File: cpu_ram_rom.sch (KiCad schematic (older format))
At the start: 10 parts, among them SW2 Reset, U6 SRAM - IS62C5128BL-45TLI, U7 SST39SF040, U8 CPU -Z84C0020AEG, U9 DS1813R-5+T&R

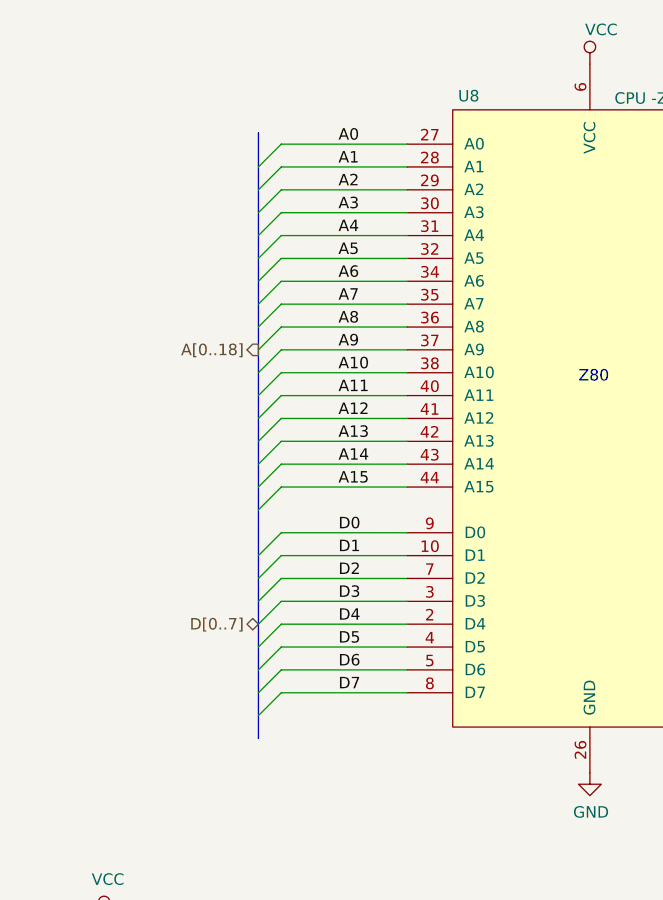
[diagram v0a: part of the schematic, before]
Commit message: fixed bus connections
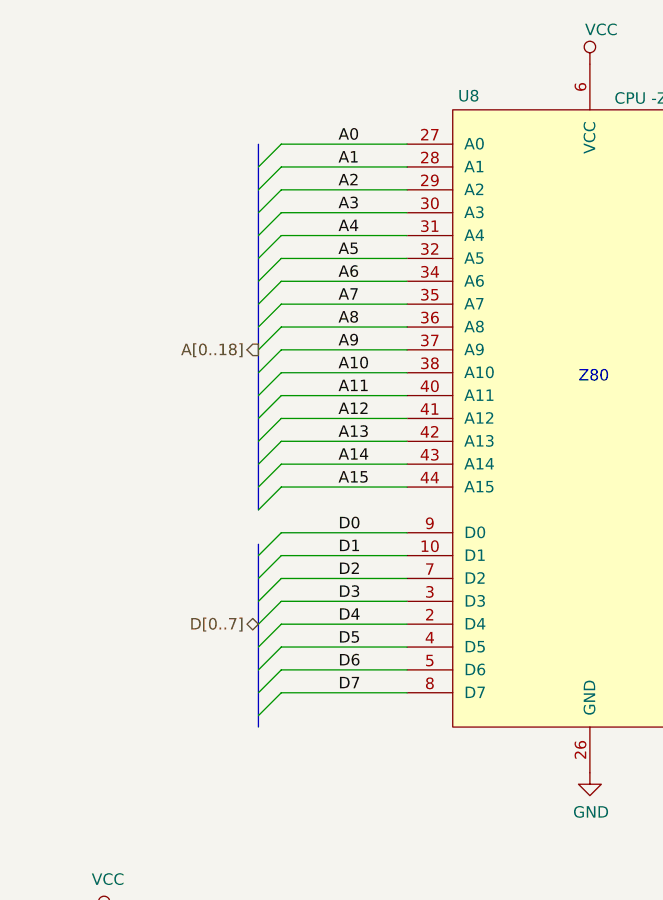
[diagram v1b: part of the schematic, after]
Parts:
- SW2: footprint Button_Switch_SMD:SW_Push_SPST_NO_Alps_SKRK -> Button_Switch_SMD:SW_SPST_FSMSM
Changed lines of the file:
@@
 F 0 "SW2" V 4004 5913 50  0000 L CNN
 F 1 "Reset" V 4095 5913 50  0000 L CNN
-F 2 "Button_Switch_SMD:SW_Push_SPST_NO_Alps_SKRK" H 4050 5965 50  0001 C CNN
+F 2 "Button_Switch_SMD:SW_SPST_FSMSM" H 4050 5965 50  0001 C CNN
 F 3 "~" H 4050 5965 50  0001 C CNN
 	1    4050 5765
@@
 ROM_~CE~
 Wire Bus Line
-	2000 1500 2000 4150
+	2000 3300 2000 4100
+Wire Bus Line
+	2000 1550 2000 3150
 $EndSCHEMATC

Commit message: passed DRC
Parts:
- removed R54, R55, R56, R57: 10K, Resistor_SMD:R_0603_1608Metric_Pad1.05x0.95mm_HandSolder, symbol Device:R_Small
- removed SW2: Reset, Button_Switch_SMD:SW_SPST_FSMSM, symbol Switch:SW_Push
- removed U6: SRAM - IS62C5128BL-45TLI, Package_SO:TSOP-II-32_21.0x10.2mm_P1.27mm, symbol THS-80:IS62C5128BL-45TLI
- removed U8: CPU -Z84C0020AEG, Package_QFP:LQFP-44_10x10mm_P0.8mm, symbol THS-80:Z84C0010AEG
- removed U9: DS1813R-5+T&R, Package_TO_SOT_SMD:SOT-23, symbol THS-80:DS1813R-5+T&R
- added C16, C17, C18: 100nF, Capacitor_SMD:C_0603_1608Metric_Pad1.05x0.95mm_HandSolder, symbol Device:C_Small
- added U4: Z84C0010AEG, Package_QFP:LQFP-44_10x10mm_P0.8mm, symbol THS-80:Z84C0010AEG
- added U5: IS62C5128BL-45TLI, Package_SO:TSOP-II-32_21.0x10.2mm_P1.27mm, symbol THS-80:IS62C5128BL-45TLI
- renumbered R53 to R21, U7 to U6
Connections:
- net labels removed: RAM_~CE, ~BUSREQ
- wire segments 116 -> 104
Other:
- note removed: "SRAM 512Kx8"
- note removed: "Z80"
- moved on the sheet: R21, U6

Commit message: finished routing, drc passed
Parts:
- added D13, D14: GRN, LED_SMD:LED_0603_1608Metric_Pad1.05x0.95mm_HandSolder, symbol Device:LED
- added R19, R20: 10K, Resistor_SMD:R_0603_1608Metric_Pad1.05x0.95mm_HandSolder, symbol Device:R_Small
- added R40, R41: 360R, Resistor_SMD:R_0603_1608Metric_Pad1.05x0.95mm_HandSolder, symbol Device:R_Small
- added U12: 74HCT3G04, Package_SO:TSSOP-8_3x3mm_P0.65mm, symbol 74xGxx:74HCT3G04
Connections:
- net labels added: RAM_~CE, ROM_~CE
- wire segments 104 -> 107
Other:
- moved on the sheet: C16, C17, C18, R21, U4, U5, U6

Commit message: track cleanup, fixed slots in ground plane
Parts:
- U12: symbol 74xGxx:74HCT3G04 -> THS-80-rescue:74HCT3G04-74xGxx
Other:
- moved on the sheet: D13, D14, R19, R20, R40, R41
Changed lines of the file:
@@
 L power:GND #PWR?
 U 1 1 5D949AED
-P 9100 5150
+P 9800 5150
 AR Path="/5D84B1E0/5D949AED" Ref="#PWR?"  Part="1"
 AR Path="/5D6224DC/5D949AED" Ref="#PWR081"  Part="1"
-F 0 "#PWR081" H 9100 4900 50  0001 C CNN
-F 1 "GND" H 9105 4977 50  0000 C CNN
-F 2 "" H 9100 5150 50  0001 C CNN
-F 3 "" H 9100 5150 50  0001 C CNN
-	1    9100 5150
+F 0 "#PWR081" H 9800 4900 50  0001 C CNN
+F 1 "GND" H 9805 4977 50  0000 C CNN
+F 2 "" H 9800 5150 50  0001 C CNN
+F 3 "" H 9800 5150 50  0001 C CNN
+	1    9800 5150
 	1    0    0    -1
 $EndComp
 Wire Wire Line
-	8550 4650 7950 4650
-Text Label 8200 4650 0    50   ~ 0
+	9250 4650 8650 4650
+Text Label 8900 4650 0    50   ~ 0
 ROM_~CE
 $Comp
 L power:GND #PWR?
 U 1 1 5D949B01
-P 6550 5100
+P 6550 5150
 AR Path="/5D84B1E0/5D949B01" Ref="#PWR?"  Part="1"
 AR Path="/5D6224DC/5D949B01" Ref="#PWR078"  Part="1"
-F 0 "#PWR078" H 6550 4850 50  0001 C CNN
-F 1 "GND" H 6555 4927 50  0000 C CNN
-F 2 "" H 6550 5100 50  0001 C CNN
-F 3 "" H 6550 5100 50  0001 C CNN
-	1    6550 5100
+F 0 "#PWR078" H 6550 4900 50  0001 C CNN
+F 1 "GND" H 6555 4977 50  0000 C CNN
+F 2 "" H 6550 5150 50  0001 C CNN
+F 3 "" H 6550 5150 50  0001 C CNN
+	1    6550 5150
 	1    0    0    -1
 $EndComp
 Wire Wire Line
-	6000 4600 5400 4600
-Text Label 5650 4600 0    50   ~ 0
+	6000 4650 5400 4650
+Text Label 5650 4650 0    50   ~ 0
 RAM_~CE
 $Comp
 L Device:R_Small R?
 U 1 1 5D949B09
-P 6550 5000
+P 6550 5050
 AR Path="/5D84B1E0/5D949B09" Ref="R?"  Part="1"
 AR Path="/5D6224DC/5D949B09" Ref="R40"  Part="1"
-F 0 "R40" H 6609 5046 50  0000 L CNN
-F 1 "360R" H 6609 4955 50  0000 L CNN
-F 2 "Resistor_SMD:R_0603_1608Metric_Pad1.05x0.95mm_HandSolder" H 6550 5000 50  0001 C CNN
-F 3 "~" H 6550 5000 50  0001 C CNN
-	1    6550 5000
+F 0 "R40" H 6609 5096 50  0000 L CNN
+F 1 "360R" H 6609 5005 50  0000 L CNN
+F 2 "Resistor_SMD:R_0603_1608Metric_Pad1.05x0.95mm_HandSolder" H 6550 5050 50  0001 C CNN
+F 3 "~" H 6550 5050 50  0001 C CNN
+	1    6550 5050
 	-1   0    0    1
 $EndComp
@@
 L Device:LED D?
 U 1 1 5D949B0F
-P 6550 4750
+P 6550 4800
 AR Path="/5D84B1E0/5D949B0F" Ref="D?"  Part="1"
 AR Path="/5D6224DC/5D949B0F" Ref="D13"  Part="1"
-F 0 "D13" V 6589 4633 50  0000 R CNN
-F 1 "GRN" V 6498 4633 50  0000 R CNN
-F 2 "LED_SMD:LED_0603_1608Metric_Pad1.05x0.95mm_HandSolder" H 6550 4750 50  0001 C CNN
-F 3 "~" H 6550 4750 50  0001 C CNN
-	1    6550 4750
+F 0 "D13" V 6589 4683 50  0000 R CNN
+F 1 "GRN" V 6498 4683 50  0000 R CNN
+F 2 "LED_SMD:LED_0603_1608Metric_Pad1.05x0.95mm_HandSolder" H 6550 4800 50  0001 C CNN
+F 3 "~" H 6550 4800 50  0001 C CNN
+	1    6550 4800
 	0    -1   -1   0
 $EndComp
@@
 L Device:LED D?
 U 1 1 5D949B15
-P 9100 4800
+P 9800 4800
 AR Path="/5D84B1E0/5D949B15" Ref="D?"  Part="1"
 AR Path="/5D6224DC/5D949B15" Ref="D14"  Part="1"
-F 0 "D14" V 9139 4683 50  0000 R CNN
-F 1 "GRN" V 9048 4683 50  0000 R CNN
-F 2 "LED_SMD:LED_0603_1608Metric_Pad1.05x0.95mm_HandSolder" H 9100 4800 50  0001 C CNN
-F 3 "~" H 9100 4800 50  0001 C CNN
-	1    9100 4800
+F 0 "D14" V 9839 4683 50  0000 R CNN
+F 1 "GRN" V 9748 4683 50  0000 R CNN
+F 2 "LED_SMD:LED_0603_1608Metric_Pad1.05x0.95mm_HandSolder" H 9800 4800 50  0001 C CNN
+F 3 "~" H 9800 4800 50  0001 C CNN
+	1    9800 4800
 	0    -1   -1   0
 $EndComp
@@
 L Device:R_Small R?
 U 1 1 5D949B1B
-P 9100 5050
+P 9800 5050
 AR Path="/5D84B1E0/5D949B1B" Ref="R?"  Part="1"
 AR Path="/5D6224DC/5D949B1B" Ref="R41"  Part="1"
-F 0 "R41" H 9159 5096 50  0000 L CNN
-F 1 "360R" H 9159 5005 50  0000 L CNN
-F 2 "Resistor_SMD:R_0603_1608Metric_Pad1.05x0.95mm_HandSolder" H 9100 5050 50  0001 C CNN
-F 3 "~" H 9100 5050 50  0001 C CNN
-	1    9100 5050
+F 0 "R41" H 9859 5096 50  0000 L CNN
+F 1 "360R" H 9859 5005 50  0000 L CNN
+F 2 "Resistor_SMD:R_0603_1608Metric_Pad1.05x0.95mm_HandSolder" H 9800 5050 50  0001 C CNN
+F 3 "~" H 9800 5050 50  0001 C CNN
+	1    9800 5050
 	-1   0    0    1
 $EndComp
@@
 L Device:R_Small R20
 U 1 1 5D959555
-P 7950 4550
-F 0 "R20" H 8009 4596 50  0000 L CNN
-F 1 "10K" H 8009 4505 50  0000 L CNN
-F 2 "Resistor_SMD:R_0603_1608Metric_Pad1.05x0.95mm_HandSolder" H 7950 4550 50  0001 C CNN
-F 3 "~" H 7950 4550 50  0001 C CNN
-	1    7950 4550
+P 8650 4550
+F 0 "R20" H 8709 4596 50  0000 L CNN
+F 1 "10K" H 8709 4505 50  0000 L CNN
+F 2 "Resistor_SMD:R_0603_1608Metric_Pad1.05x0.95mm_HandSolder" H 8650 4550 50  0001 C CNN
+F 3 "~" H 8650 4550 50  0001 C CNN
+	1    8650 4550
 	1    0    0    -1
 $EndComp
@@
 L power:VCC #PWR042
 U 1 1 5D95955B
-P 7950 4450
-F 0 "#PWR042" H 7950 4300 50  0001 C CNN
-F 1 "VCC" H 7950 4600 50  0000 C CNN
-F 2 "" H 7950 4450 50  0001 C CNN
-F 3 "" H 7950 4450 50  0001 C CNN
-	1    7950 4450
+P 8650 4450
+F 0 "#PWR042" H 8650 4300 50  0001 C CNN
+F 1 "VCC" H 8650 4600 50  0000 C CNN
+F 2 "" H 8650 4450 50  0001 C CNN
+F 3 "" H 8650 4450 50  0001 C CNN
+	1    8650 4450
 	1    0    0    -1
 $EndComp
@@
 L Device:R_Small R19
 U 1 1 5D966170
-P 5400 4500
-F 0 "R19" H 5459 4546 50  0000 L CNN
-F 1 "10K" H 5459 4455 50  0000 L CNN
-F 2 "Resistor_SMD:R_0603_1608Metric_Pad1.05x0.95mm_HandSolder" H 5400 4500 50  0001 C CNN
-F 3 "~" H 5400 4500 50  0001 C CNN
-	1    5400 4500
+P 5400 4550
+F 0 "R19" H 5459 4596 50  0000 L CNN
+F 1 "10K" H 5459 4505 50  0000 L CNN
+F 2 "Resistor_SMD:R_0603_1608Metric_Pad1.05x0.95mm_HandSolder" H 5400 4550 50  0001 C CNN
+F 3 "~" H 5400 4550 50  0001 C CNN
+	1    5400 4550
 	1    0    0    -1
 $EndComp
@@
 L power:VCC #PWR041
 U 1 1 5D966176
-P 5400 4400
-F 0 "#PWR041" H 5400 4250 50  0001 C CNN
-F 1 "VCC" H 5400 4550 50  0000 C CNN
-F 2 "" H 5400 4400 50  0001 C CNN
-F 3 "" H 5400 4400 50  0001 C CNN
-	1    5400 4400
+P 5400 4450
+F 0 "#PWR041" H 5400 4300 50  0001 C CNN
+F 1 "VCC" H 5400 4600 50  0000 C CNN
+F 2 "" H 5400 4450 50  0001 C CNN
+F 3 "" H 5400 4450 50  0001 C CNN
+	1    5400 4450
 	1    0    0    -1
 $EndComp
 $Comp
-L 74xGxx:74HCT3G04 U12
+L THS-80-rescue:74HCT3G04-74xGxx U12
 U 2 1 5DA048AA
-P 6300 4600
-F 0 "U12" H 6275 4867 50  0000 C CNN
-F 1 "74HCT3G04" H 6275 4776 50  0000 C CNN
-F 2 "Package_SO:TSSOP-8_3x3mm_P0.65mm" H 6300 4600 50  0001 C CNN
-F 3 "https://www.mouser.com/datasheet/2/916/74HC_HCT3G04-1319126.pdf" H 6300 4600 50  0001 C CNN
-	2    6300 4600
+P 6300 4650
+AR Path="/5DA048AA" Ref="U12"  Part="2"
+AR Path="/5D6224DC/5DA048AA" Ref="U12"  Part="2"
+F 0 "U12" H 6275 4917 50  0000 C CNN
+F 1 "74HCT3G04" H 6275 4826 50  0000 C CNN
+F 2 "Package_SO:TSSOP-8_3x3mm_P0.65mm" H 6300 4650 50  0001 C CNN
+F 3 "https://www.mouser.com/datasheet/2/916/74HC_HCT3G04-1319126.pdf" H 6300 4650 50  0001 C CNN
+	2    6300 4650
 	1    0    0    -1
 $EndComp
@@
 ~WR
 $Comp
-L 74xGxx:74HCT3G04 U?
+L THS-80-rescue:74HCT3G04-74xGxx U?
 U 1 1 5DA6489D
-P 8850 4650
+P 9550 4650
 AR Path="/5D70CA34/5DA6489D" Ref="U?"  Part="1"
 AR Path="/5D6224DC/5DA6489D" Ref="U12"  Part="1"
-F 0 "U12" H 8825 4917 50  0000 C CNN
-F 1 "74HCT3G04" H 8825 4826 50  0000 C CNN
-F 2 "Package_SO:TSSOP-8_3x3mm_P0.65mm" H 8850 4650 50  0001 C CNN
-F 3 "https://www.mouser.com/datasheet/2/916/74HC_HCT3G04-1319126.pdf" H 8850 4650 50  0001 C CNN
-	1    8850 4650
+AR Path="/5DA6489D" Ref="U12"  Part="1"
+F 0 "U12" H 9525 4917 50  0000 C CNN
+F 1 "74HCT3G04" H 9525 4826 50  0000 C CNN
+F 2 "Package_SO:TSSOP-8_3x3mm_P0.65mm" H 9550 4650 50  0001 C CNN
+F 3 "https://www.mouser.com/datasheet/2/916/74HC_HCT3G04-1319126.pdf" H 9550 4650 50  0001 C CNN
+	1    9550 4650
 	1    0    0    -1
 $EndComp

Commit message: lots of fixes
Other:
- moved on the sheet: C16, C17, C18, D13, D14, R19, R20, R21, R40, R41, U12A, U12B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

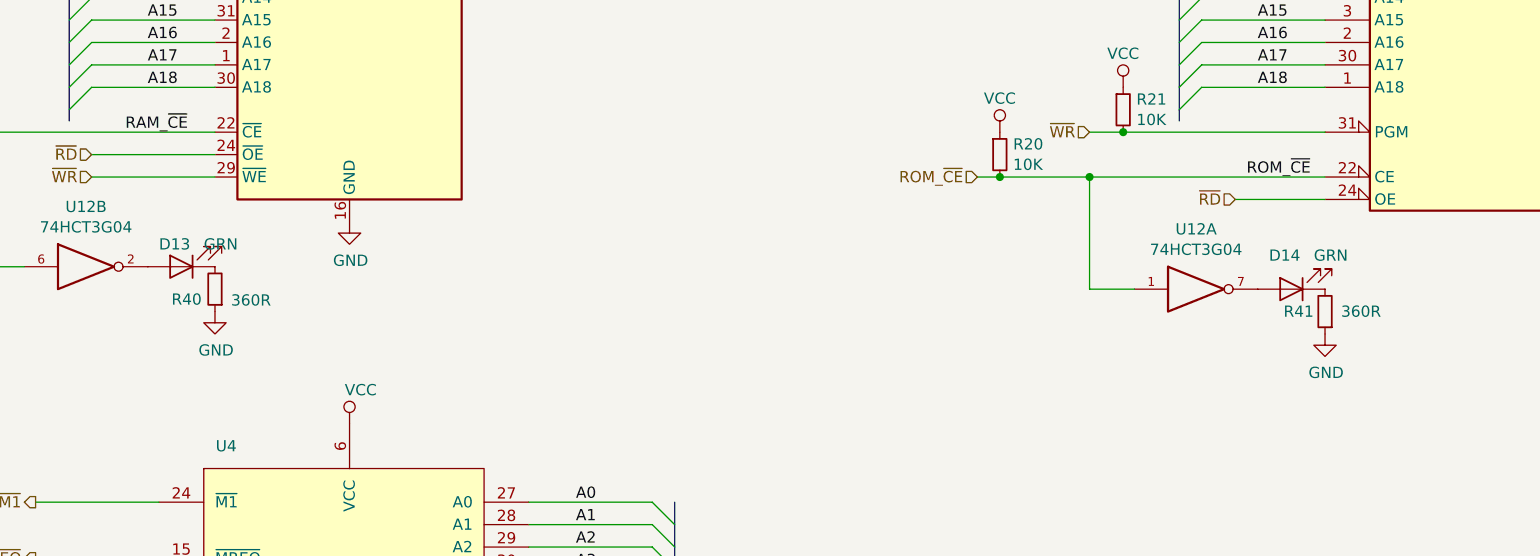
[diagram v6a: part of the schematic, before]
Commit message: fixed led values, added pwr led
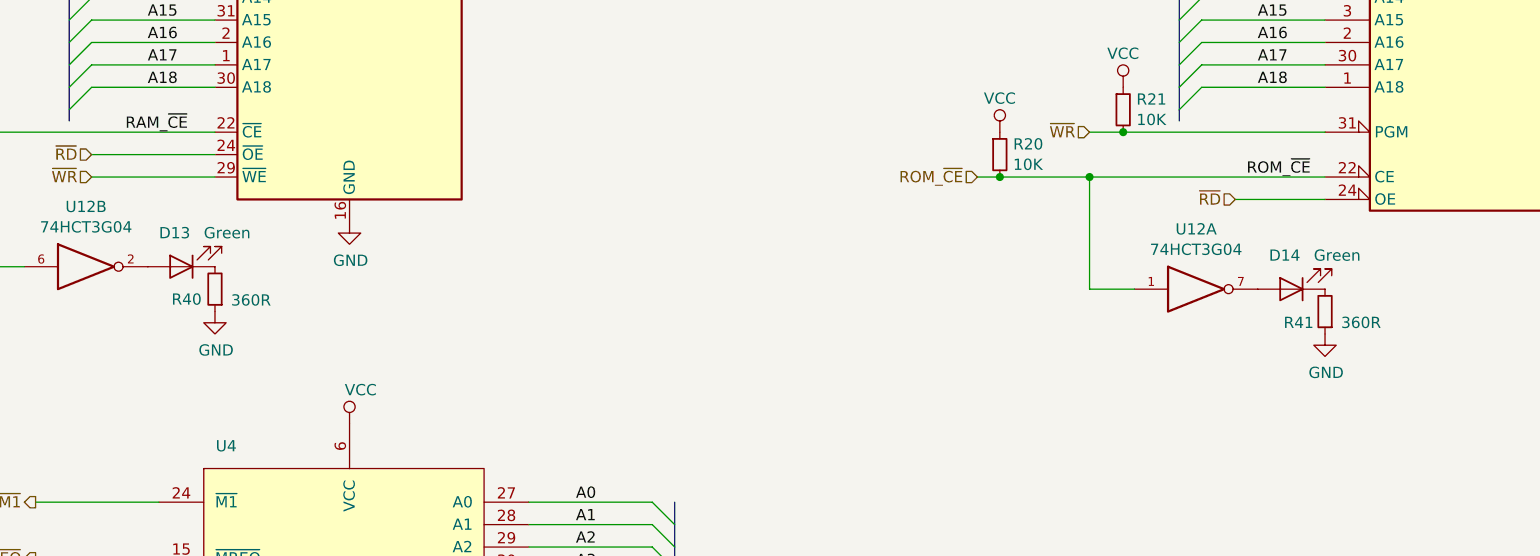
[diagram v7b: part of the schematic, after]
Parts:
- D13, D14: value GRN -> Green
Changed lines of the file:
@@
 AR Path="/5D84B1E0/5D949B0F" Ref="D?"  Part="1"
 AR Path="/5D6224DC/5D949B0F" Ref="D13"  Part="1"
-F 0 "D13" H 3000 3500 50  0000 R CNN
-F 1 "GRN" H 2800 3500 50  0000 R CNN
+F 0 "D13" H 3000 3450 50  0000 R CNN
+F 1 "Green" H 2800 3450 50  0000 R CNN
 F 2 "LED_SMD:LED_0603_1608Metric_Pad1.05x0.95mm_HandSolder" H 2900 3600 50  0001 C CNN
 F 3 "~" H 2900 3600 50  0001 C CNN
@@
 AR Path="/5D6224DC/5D949B15" Ref="D14"  Part="1"
 F 0 "D14" H 7950 3550 50  0000 R CNN
-F 1 "GRN" H 7750 3550 50  0000 R CNN
+F 1 "Green" H 7750 3550 50  0000 R CNN
 F 2 "LED_SMD:LED_0603_1608Metric_Pad1.05x0.95mm_HandSolder" H 7850 3700 50  0001 C CNN
 F 3 "~" H 7850 3700 50  0001 C CNN
@@
 AR Path="/5D84B1E0/5D949B1B" Ref="R?"  Part="1"
 AR Path="/5D6224DC/5D949B1B" Ref="R41"  Part="1"
-F 0 "R41" H 8050 3800 50  0000 L CNN
-F 1 "360R" H 7750 3800 50  0000 L CNN
+F 0 "R41" H 8050 3850 50  0000 L CNN
+F 1 "360R" H 7750 3850 50  0000 L CNN
 F 2 "Resistor_SMD:R_0603_1608Metric_Pad1.05x0.95mm_HandSolder" H 8000 3800 50  0001 C CNN
 F 3 "~" H 8000 3800 50  0001 C CNN
